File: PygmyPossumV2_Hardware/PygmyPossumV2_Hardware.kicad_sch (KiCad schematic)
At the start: 28 parts, among them U1 BISS0001

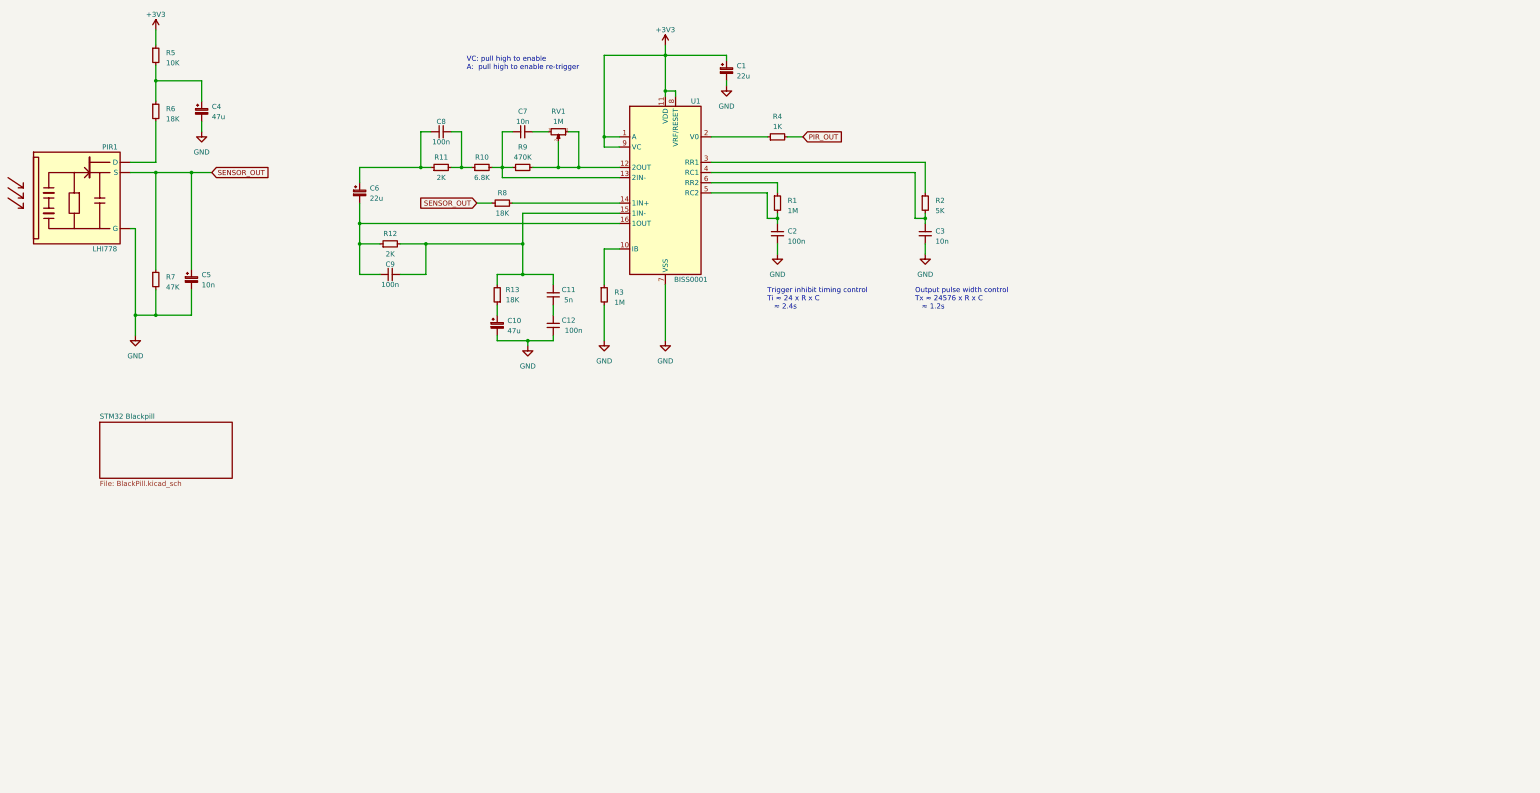
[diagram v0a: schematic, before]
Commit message: Rename project, add MCU circuitry
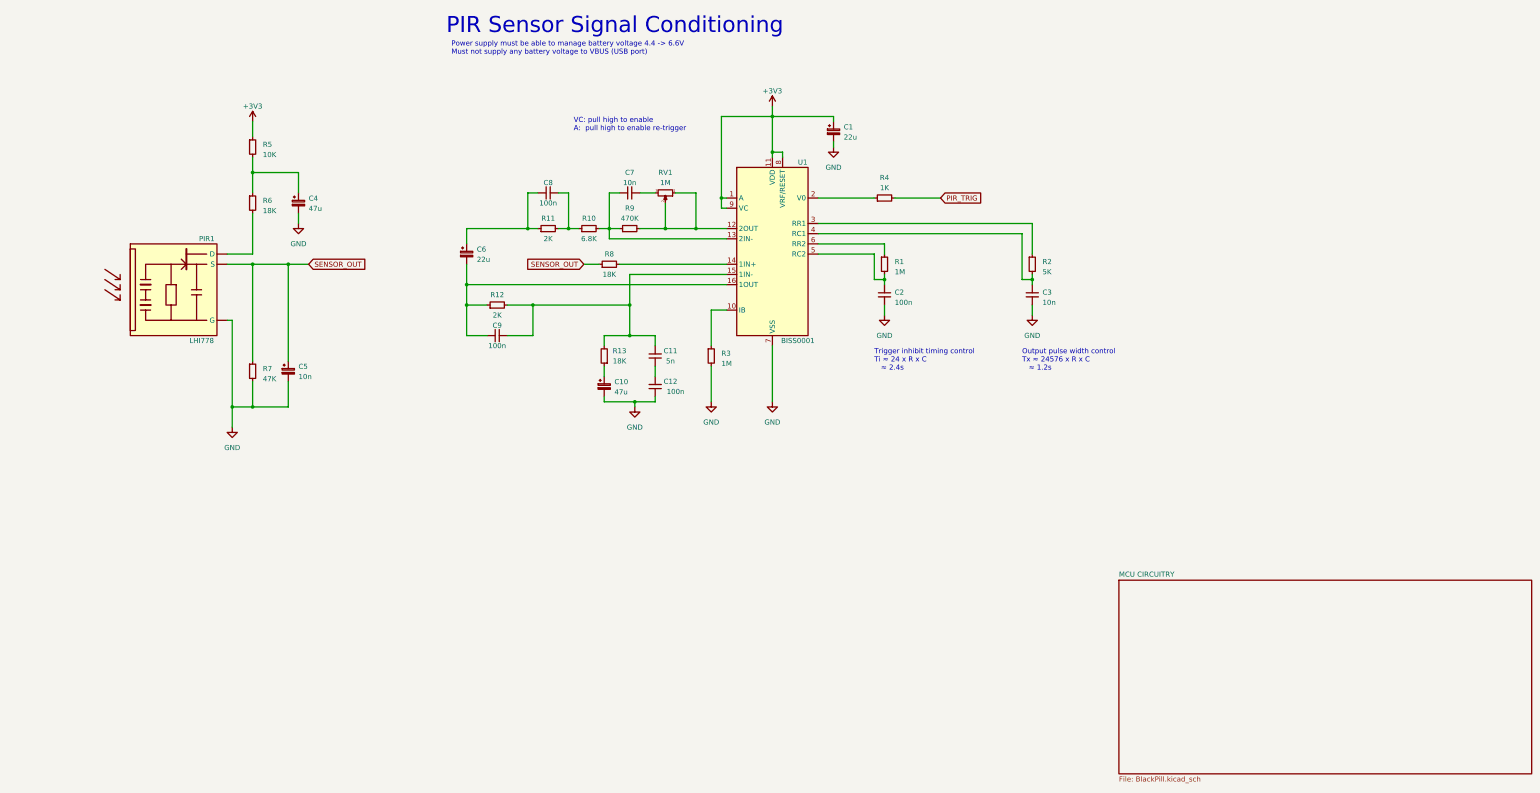
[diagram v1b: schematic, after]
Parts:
- C1, C10, C4, C5, C6: footprint (none) -> Capacitor_SMD:CP_Elec_4x5.4
- C11, C12, C2, C3, C7, C8, C9: footprint (none) -> Capacitor_SMD:C_0402_1005Metric
- R1, R10, R11, R12, R13, R2, R3, R4, R5, R6, R7, R8, R9: footprint (none) -> Resistor_SMD:R_0402_1005Metric
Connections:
- net PIR_OUT renamed PIR_TRIG
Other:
- sheet STM32 Blackpill renamed MCU CIRCUITRY
- note added: "PIR Sensor Signal Conditioning"
- note added: "Power supply must be able to manage battery voltage 4.4 -> 6.6V Must not supply any battery voltage to VBUS (USB port)"
- company: (none) -> BanksiaBytes
- title: (none) -> PYGMY POSSUM
- moved on the sheet: C1, C10, C11, C12, C2, C3, C4, C5, C6, C7, C8, C9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
